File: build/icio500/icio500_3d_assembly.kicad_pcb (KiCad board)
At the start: 4 copper layers, 150.8 x 114.3 mm, 57 parts, among them J1 ?, U1 ?, U2 ?, U3 ?, U4 ?, U5 ?, U6 ?

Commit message: Update assembly file to include new right-angle U6 position
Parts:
- U6: footprint Connector_PinHeader_2.54mm:PinHeader_2x10_P2.54mm_Vertical -> Connector_PinHeader_2.54mm:PinHeader_2x10_P2.54mm_Horizontal
- moved U6 43.3 mm to (52.2, 120.5), turned to 180 degrees
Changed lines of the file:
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@@
 		)
 	)
-	(footprint "Connector_PinHeader_2.54mm:PinHeader_2x10_P2.54mm_Vertical"
+	(footprint "Connector_PinHeader_2.54mm:PinHeader_2x10_P2.54mm_Horizontal"
 		(layer "F.Cu")
-		(at 93.37 107 90)
+		(at 52.17 120.475 180)
 		(descr "Through hole straight pin header, 2x10, 2.54mm pitch, double rows")
 		(tags "Through hole pin header THT 2x10 2.54mm double row")
@@
 		)
 		(embedded_fonts no)
-		(model "${KICAD10_3DMODEL_DIR}/Connector_PinHeader_2.54mm.3dshapes/PinHeader_2x10_P2.54mm_Vertical.step"
+		(model "/Connector_PinHeader_2.54mm.3dshapes/PinHeader_2x10_P2.54mm_Horizontal.step"
 			(offset
 				(xyz 0 0 0)
@@
 		)
 	)
-	  (footprint "DUMMY"
+  (footprint "DUMMY"
     (layer "F.Cu")
     (at 52.17 112.15)
@@
     )
   )
-  (embedded_fonts no)
+(embedded_fonts no)
 )

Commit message: Fix final mechanical alignments: Sync assembly file, fix U6 Y-axis inversion, use exact zero-origin STEP exports
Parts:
- moved U6 16.6 mm to (52.2, 103.8)
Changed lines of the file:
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@@
 	(footprint "Connector_PinHeader_2.54mm:PinHeader_2x10_P2.54mm_Horizontal"
 		(layer "F.Cu")
-		(at 52.17 120.475 180)
+		(at 52.17 103.825 180)
 		(descr "Through hole straight pin header, 2x10, 2.54mm pitch, double rows")
 		(tags "Through hole pin header THT 2x10 2.54mm double row")

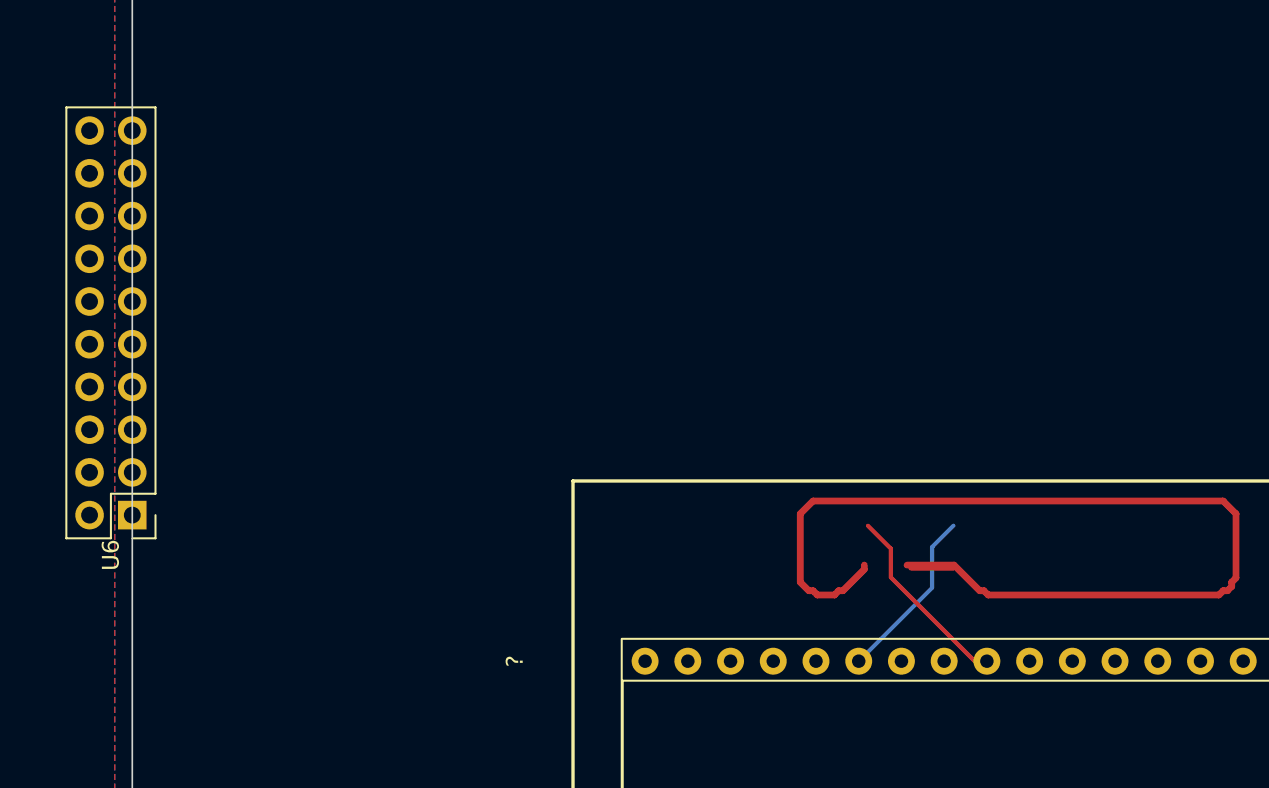
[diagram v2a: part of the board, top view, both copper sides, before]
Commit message: Fix 3D offsets finally (Offset AFTER rotation) and autoroute main board U6 connections
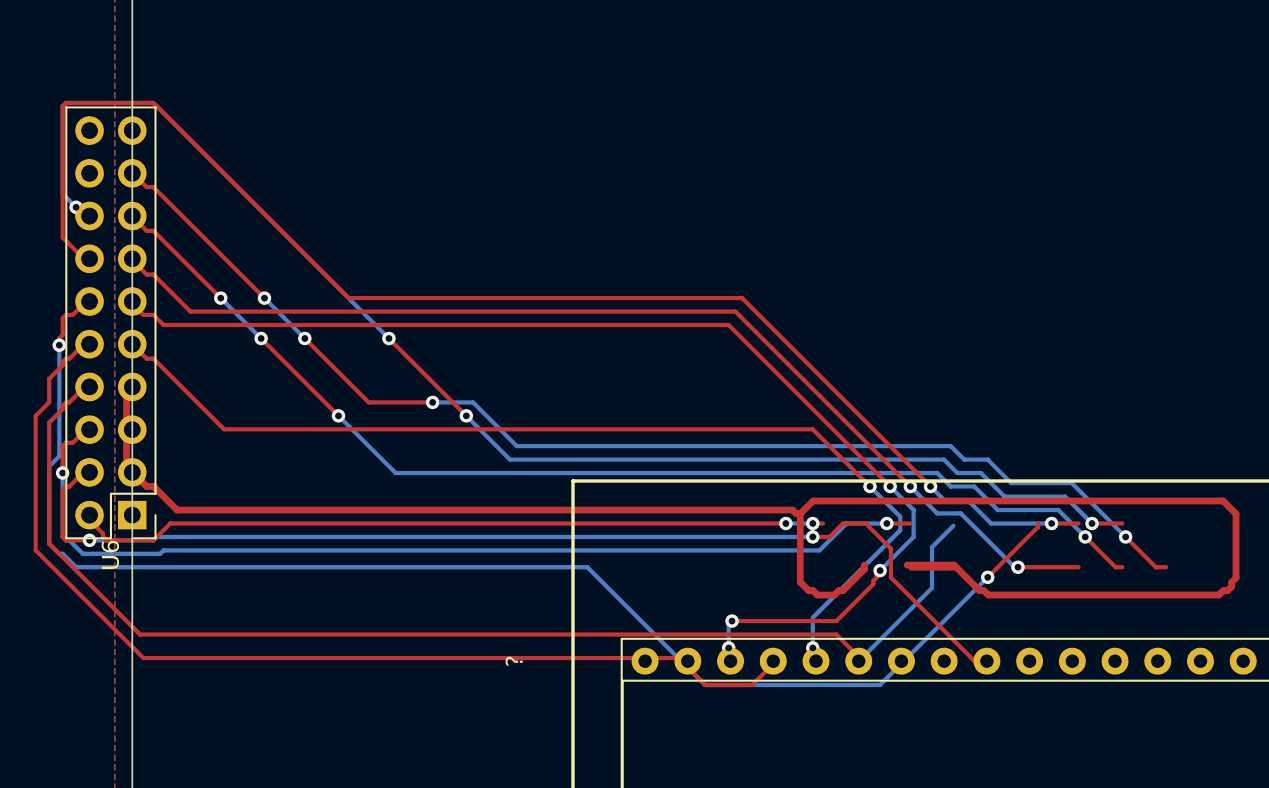
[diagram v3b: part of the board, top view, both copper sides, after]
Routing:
- net spi1_mosi: track 8.87 -> 91.0 mm
- net spi1_sck: track 9.93 -> 90.7 mm
- net gpio_disp_dc: track 11.4 -> 92.2 mm
- net gpio_disp_res: track 9.35 -> 80.7 mm
- net gpio_enc_sw: track 20.6 -> 89.3 mm
- net spi1_cs: track 7.39 -> 75.1 mm
- net spi1_miso: track 6.33 -> 70.4 mm
- net gpio_enc_b: track 17.1 -> 79.1 mm
- net d13: track 10.4 -> 71.9 mm
- net d14: track 14.4 -> 75.1 mm
- net i2c1_scl: track 16.0 -> 75.0 mm
- net i2c1_sda: track 11.4 -> 64.6 mm
- net gnd: track 223.5 -> 269.1 mm
- net audio_in_r: track 49.6 -> 94.6 mm
- net 0: vias 0 -> 30

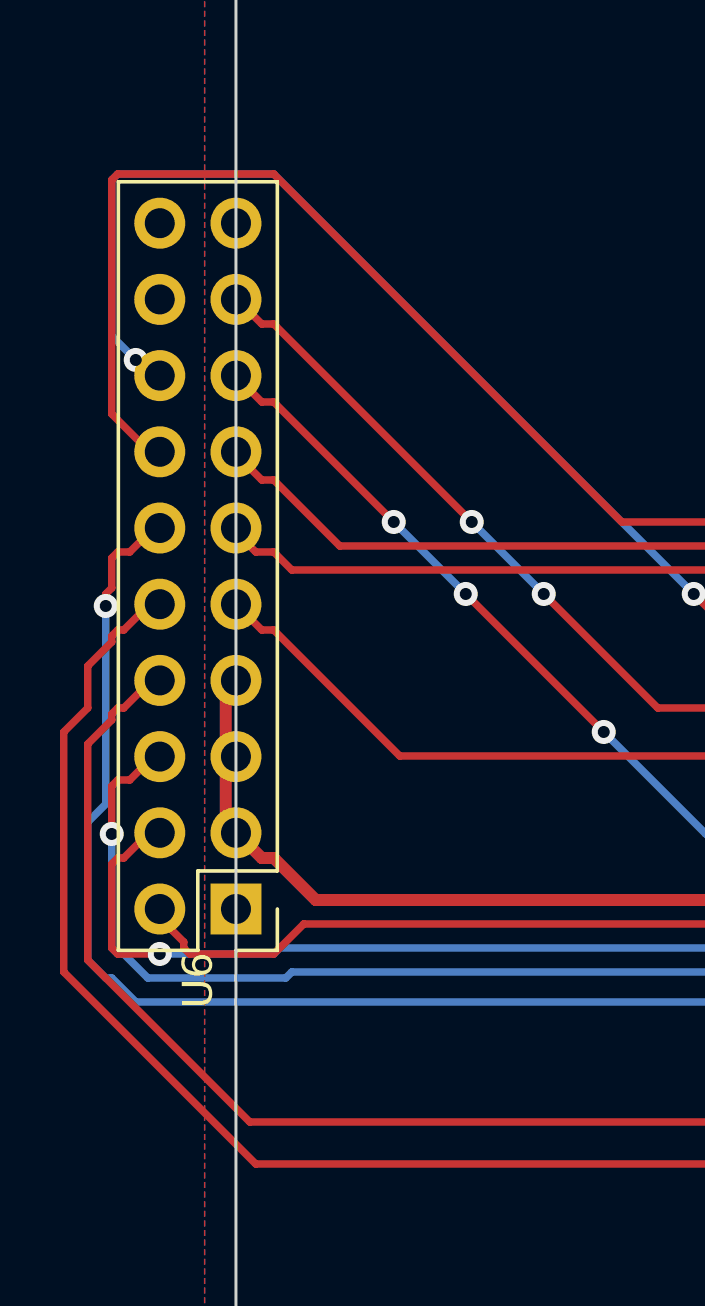
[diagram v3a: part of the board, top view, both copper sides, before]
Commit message: Move U6 to X=56.0, reconnect perfectly, and finalize exact GUI 3D offsets
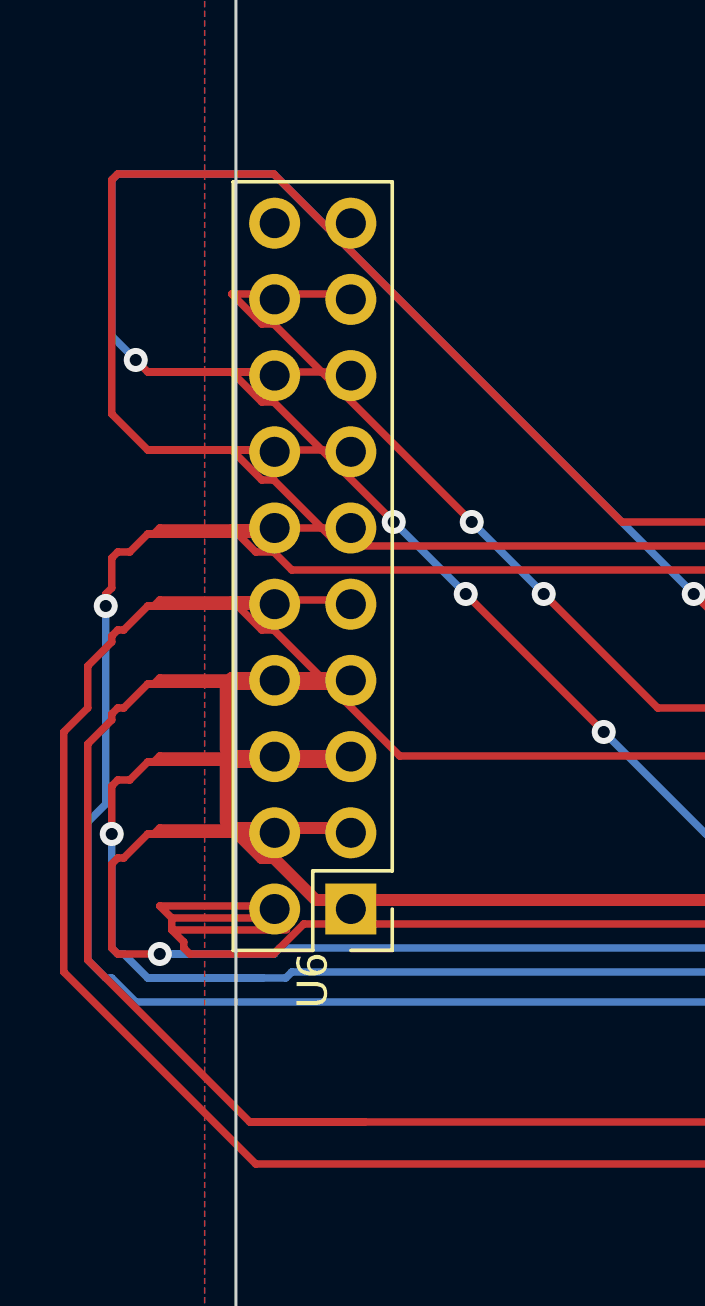
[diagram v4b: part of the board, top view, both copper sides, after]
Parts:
- moved U6 3.83 mm to (56.0, 103.8)
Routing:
- net gnd: track 269.1 -> 288.3 mm
- net i2c1_sda: track 64.6 -> 79.9 mm
- net i2c1_scl: track 75.0 -> 90.3 mm
- net d13: track 71.9 -> 87.3 mm
- net spi1_mosi: track 91.0 -> 102.5 mm
- net gpio_enc_b: track 79.1 -> 90.6 mm
- net audio_in_r: track 94.6 -> 106.1 mm
- net gpio_disp_dc: track 92.2 -> 99.8 mm
- net spi1_sck: track 90.7 -> 98.3 mm
- net gpio_disp_res: track 80.7 -> 84.6 mm
- net spi1_miso: track 70.4 -> 74.2 mm
- net spi1_cs: track 75.1 -> 78.9 mm
- net gpio_enc_sw: track 89.3 -> 93.2 mm
- net d14: track 75.1 -> 78.9 mm
